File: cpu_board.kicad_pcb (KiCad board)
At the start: 2 copper layers, 130 x 75 mm, 36 parts, among them J1 POWER, J2 UART, J3 I2C, J4 GPIOA, J5 GPIOB, J6 GPIOC, SW1 RESET, U1 TL7705A, U2 W65C02SxP, U3 AS6C62256-55PCN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

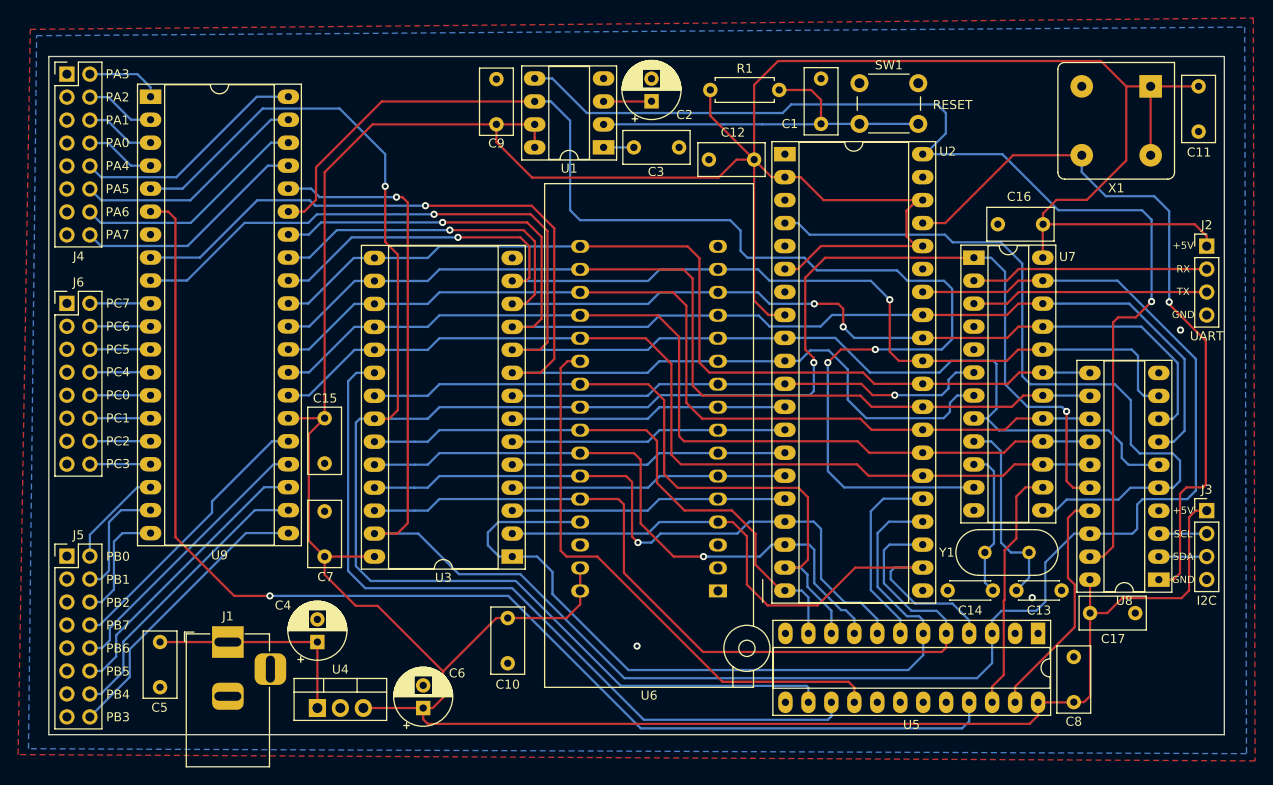
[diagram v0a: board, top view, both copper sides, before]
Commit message: Fix capacitors footprints & add POWER header
Signed-off-by: Arnaud Ferraris <arnaud.ferraris@gmail.com>
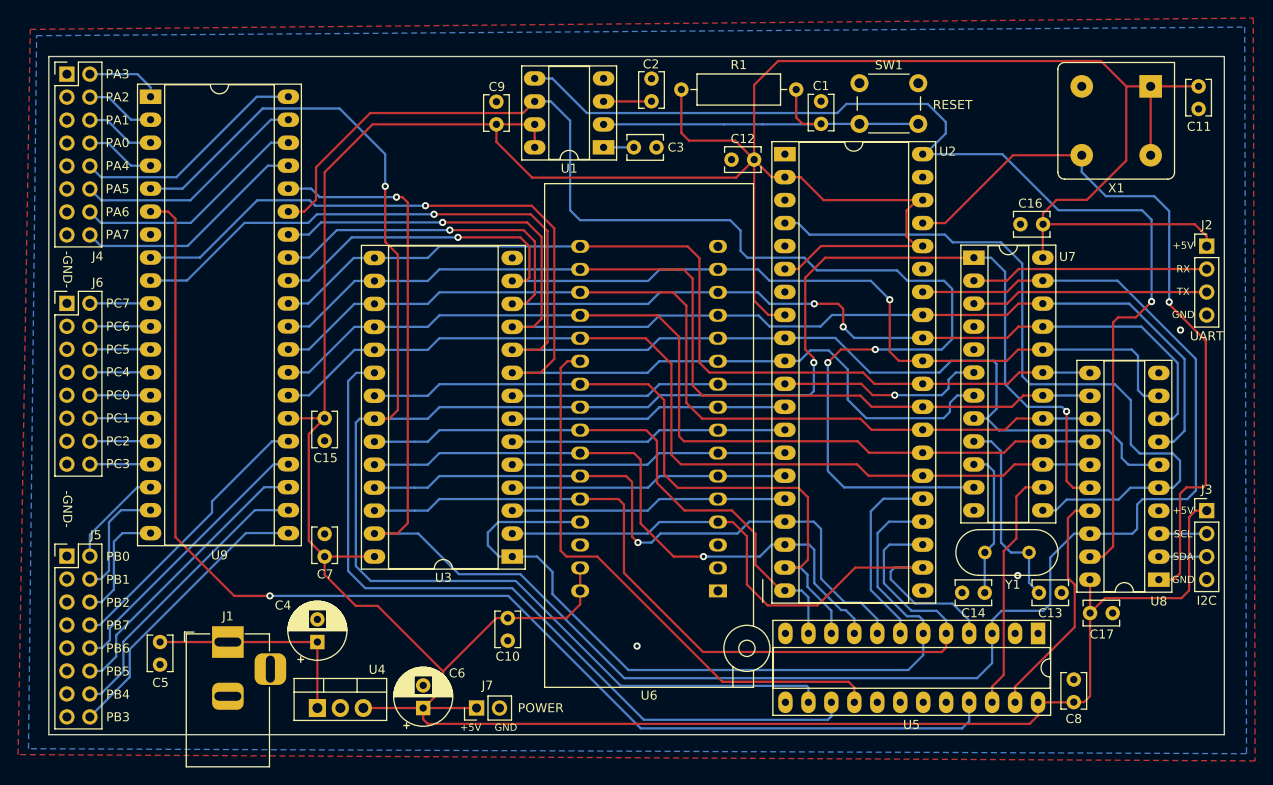
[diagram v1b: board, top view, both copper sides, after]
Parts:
- added J7: POWER, Connector_PinHeader_2.54mm:PinHeader_1x02_P2.54mm_Vertical, F.Cu at (132.1, 126.9)
- C1, C10, C11, C12, C15, C16, C17, C3, C5, C7, C8, C9: footprint Capacitor_THT:C_Rect_L7.2mm_W3.5mm_P5.00mm_FKS2_FKP2_MKS2_MKP2 -> Capacitor_THT:C_Disc_D3.8mm_W2.6mm_P2.50mm
- C13, C14: footprint Capacitor_THT:C_Disc_D4.3mm_W1.9mm_P5.00mm -> Capacitor_THT:C_Disc_D3.8mm_W2.6mm_P2.50mm
- C2: value 1µ -> 100n; footprint Capacitor_THT:CP_Radial_D6.3mm_P2.50mm -> Capacitor_THT:C_Disc_D3.8mm_W2.6mm_P2.50mm
- R1: footprint Resistor_THT:R_Axial_DIN0207_L6.3mm_D2.5mm_P7.62mm_Horizontal -> Resistor_THT:R_Axial_DIN0309_L9.0mm_D3.2mm_P12.70mm_Horizontal
- moved R1 3.20 mm to (154.7, 58.5)
- moved C14 0.93 mm to (188.2, 114.2)
- moved C13 0.25 mm to (196.8, 114.2)
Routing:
- net +5V: track 466.2 -> 475.8 mm
- net Net-(C1-Pad1): track 42.5 -> 40.9 mm
- net /~RST~: track 124.0 -> 123.4 mm
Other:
- board text added: "-GND-"

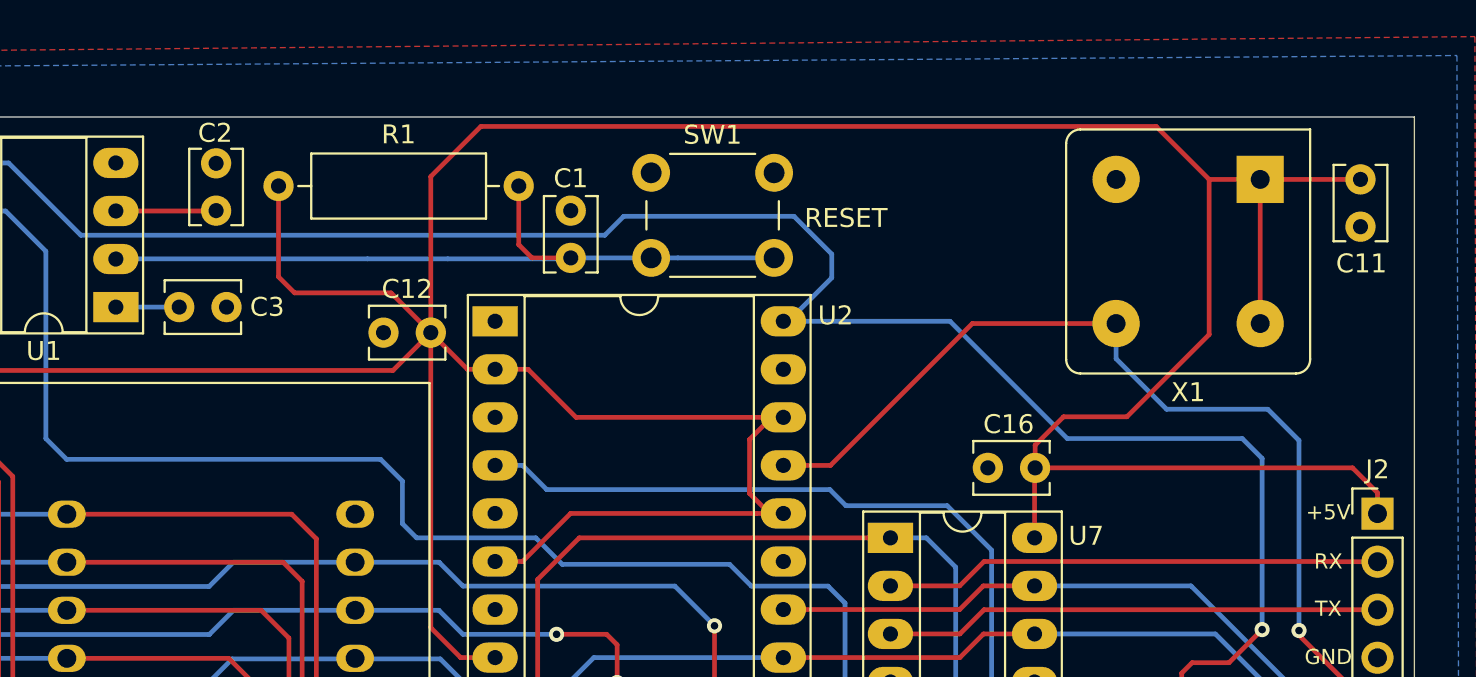
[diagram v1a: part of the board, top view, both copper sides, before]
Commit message: Add pull-ups for unused CPU inputs
Signed-off-by: Arnaud Ferraris <arnaud.ferraris@gmail.com>
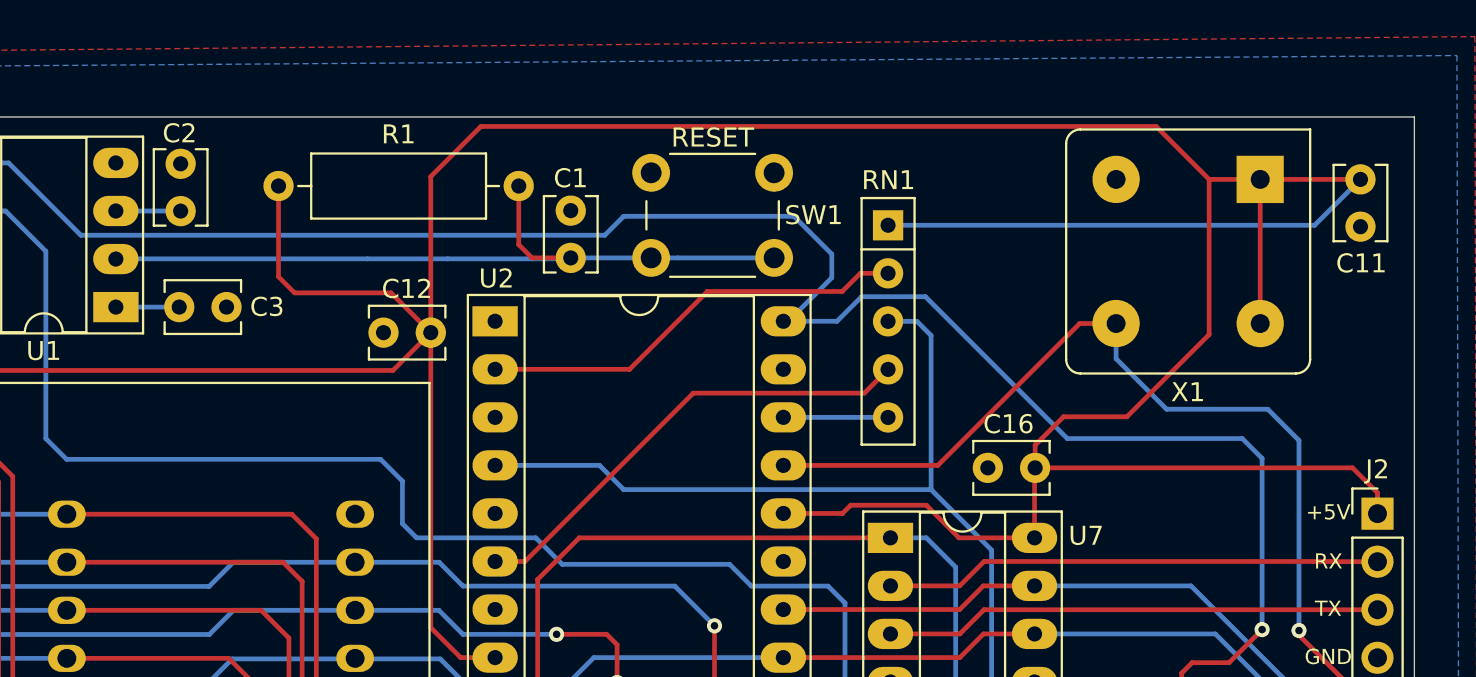
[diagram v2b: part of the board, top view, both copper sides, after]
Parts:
- added RN1: 3.3K, Resistor_THT:R_Array_SIP5, F.Cu at (186.9, 60.6)
- moved C2 1.88 mm to (149.5, 59.8)
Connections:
- U2 pad 2: +5V -> /RDY
- U2 pad 38: +5V -> /~SO~
- U2 pad 6: +5V -> /~NMI~
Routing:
- net /~NMI~: track 0.00 -> 25.0 mm
- net /RDY: track 0.00 -> 22.9 mm
- net /~IRQ~: track 83.5 -> 94.2 mm
- net /~SO~: track 0.00 -> 5.54 mm
- net +5V: track 475.8 -> 471.9 mm
- net Net-(C2-Pad1): track 5.31 -> 3.43 mm
- net /~RST~: track 123.4 -> 124.5 mm
